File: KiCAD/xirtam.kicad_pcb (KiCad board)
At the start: 2 copper layers, 71.1 x 51.8 mm, 29 parts, among them J1 Exp Header, J2 Matrix, J3 Power, J4 JTAG, J5 Bootloader, P1 USB_A, SW1 Reset, U1 MT093APR1, U2 AT90USB1287, Y1 16 MHz Crystal

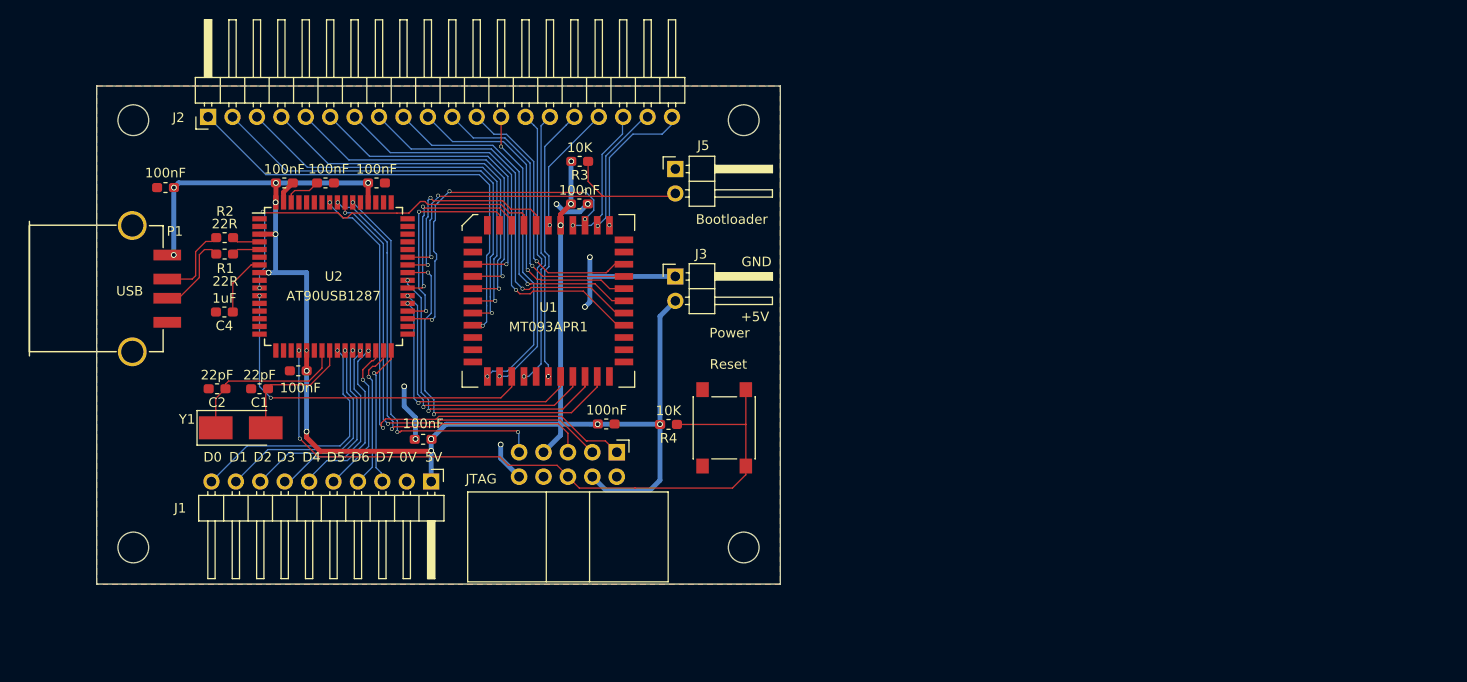
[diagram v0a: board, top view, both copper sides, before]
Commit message: Add in-line connector layout to PCB, no routing
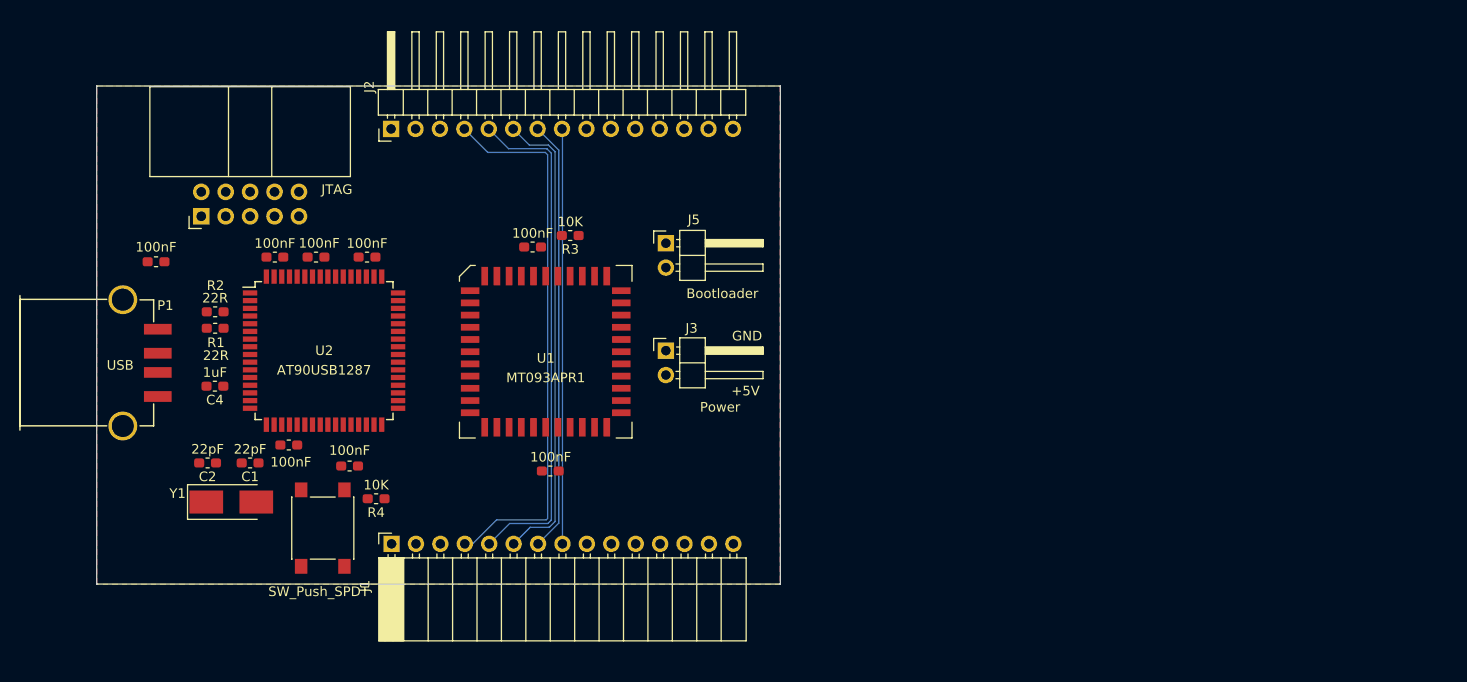
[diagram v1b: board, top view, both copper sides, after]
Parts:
- removed REF** (x4): MountingHole_3.2mm_M3, MountingHole:MountingHole_3.2mm_M3
- J1: value Exp Header -> Conn_01x15_Female; footprint Connector_PinHeader_2.54mm:PinHeader_1x10_P2.54mm_Horizontal -> Connector_PinSocket_2.54mm:PinSocket_1x15_P2.54mm_Horizontal
- J2: value Matrix -> Conn_01x15_Male; footprint Connector_PinHeader_2.54mm:PinHeader_1x20_P2.54mm_Horizontal -> Connector_PinHeader_2.54mm:PinHeader_1x15_P2.54mm_Horizontal
- SW1: value Reset -> SW_Push_SPDT
- moved J4 49.7 mm to (131.5, 93.8), turned to 90 degrees
- moved SW1 43.0 mm to (144.2, 126.3), turned to 90 degrees
- moved R4 31.4 mm to (149.7, 123.2)
- moved J2 19.1 mm to (151.3, 84.7)
- moved C8 8.14 mm to (147.0, 119.8)
- moved C6 7.78 mm to (140.6, 117.6)
- moved C9 7.78 mm to (126.8, 98.5)
- moved J3 7.78 mm to (179.9, 107.8)
- moved P1 7.78 mm to (125.5, 109.1)
- moved R1 7.78 mm to (133.0, 105.5)
- moved U2 7.78 mm to (144.3, 107.8)
- moved Y1 7.78 mm to (134.7, 123.5)
- moved R3 7.78 mm to (169.9, 95.8)
- moved C1 7.78 mm to (136.6, 119.5)
- moved C10 7.78 mm to (148.8, 98.1)
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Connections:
- J1 pad 1: +5V -> Net-(J1-Pad1)
- J1 pad 2: GND -> Net-(J1-Pad2)
- J2 pad 1: Net-(J2-Pad1) -> Net-(J1-Pad1)
- J2 pad 10: Net-(J2-Pad10) -> Net-(J1-Pad10)
- J2 pad 11: Net-(J2-Pad11) -> Net-(J1-Pad11)
- J2 pad 12: Net-(J2-Pad12) -> Net-(J1-Pad12)
- J2 pad 13: Net-(J2-Pad13) -> Net-(J1-Pad13)
- J2 pad 14: Net-(J2-Pad14) -> Net-(J1-Pad14)
- J2 pad 15: Net-(J2-Pad15) -> Net-(J1-Pad15)
- J2 pad 2: Net-(J2-Pad2) -> Net-(J1-Pad2)
- J2 pad 3: Net-(J2-Pad3) -> Net-(J1-Pad3)
- J2 pad 4: Net-(J2-Pad4) -> Net-(J1-Pad4)
- J2 pad 5: Net-(J2-Pad5) -> Net-(J1-Pad5)
- J2 pad 6: Net-(J2-Pad6) -> Net-(J1-Pad6)
- J2 pad 7: Net-(J2-Pad7) -> Net-(J1-Pad7)
- J2 pad 8: Net-(J2-Pad8) -> Net-(J1-Pad8)
- J2 pad 9: Net-(J2-Pad9) -> Net-(J1-Pad9)
- J4 pad 8: Net-(J4-Pad8) -> (no net)
- U1 pad 1: Net-(J2-Pad17) -> Net-(J1-Pad1)
- U1 pad 10: Net-(J2-Pad5) -> (no net)
- U1 pad 11: Net-(J2-Pad4) -> (no net)
- U1 pad 12: Net-(J2-Pad3) -> (no net)
- U1 pad 13: Net-(J2-Pad2) -> (no net)
- U1 pad 14: Net-(J2-Pad1) -> (no net)
- U1 pad 18: Net-(J2-Pad13) -> Net-(J1-Pad2)
- U1 pad 19: Net-(J2-Pad14) -> Net-(J1-Pad3)
- U1 pad 21: Net-(J2-Pad15) -> Net-(J1-Pad4)
- U1 pad 23: Net-(J2-Pad16) -> Net-(J1-Pad5)
- U1 pad 32: Net-(J2-Pad7) -> Net-(J1-Pad8)
- U1 pad 33: Net-(J2-Pad8) -> Net-(J1-Pad9)
- U1 pad 34: Net-(J2-Pad9) -> Net-(J1-Pad12)
- U1 pad 35: Net-(J2-Pad10) -> Net-(J1-Pad13)
- U1 pad 36: Net-(J2-Pad11) -> Net-(J1-Pad14)
- U1 pad 37: Net-(J2-Pad12) -> Net-(J1-Pad15)
- U1 pad 40: Net-(J2-Pad20) -> Net-(J1-Pad7)
- U1 pad 41: Net-(J2-Pad19) -> Net-(J1-Pad10)
- U1 pad 43: Net-(J2-Pad18) -> Net-(J1-Pad11)
- U1 pad 9: Net-(J2-Pad6) -> Net-(J1-Pad6)
- U2 pad 1: Net-(U2-Pad1) -> (no net)
- U2 pad 12: Net-(U2-Pad12) -> (no net)
- U2 pad 13: Net-(U2-Pad13) -> (no net)
- U2 pad 14: Net-(U2-Pad14) -> (no net)
- U2 pad 15: Net-(U2-Pad15) -> (no net)
- U2 pad 16: Net-(U2-Pad16) -> (no net)
- U2 pad 17: Net-(U2-Pad17) -> (no net)
- U2 pad 18: Net-(U2-Pad18) -> (no net)
- U2 pad 19: Net-(U2-Pad19) -> (no net)
- U2 pad 2: Net-(U2-Pad2) -> (no net)
- U2 pad 25: Net-(J1-Pad10) -> (no net)
- U2 pad 26: Net-(J1-Pad9) -> (no net)
- U2 pad 27: Net-(J1-Pad8) -> (no net)
- U2 pad 28: Net-(J1-Pad7) -> (no net)
- U2 pad 29: Net-(J1-Pad6) -> (no net)
- U2 pad 30: Net-(J1-Pad5) -> (no net)
- U2 pad 31: Net-(J1-Pad4) -> (no net)
- U2 pad 32: Net-(J1-Pad3) -> (no net)
- U2 pad 33: Net-(U2-Pad33) -> (no net)
- U2 pad 34: Net-(U2-Pad34) -> (no net)
- U2 pad 44: Net-(U2-Pad44) -> (no net)
- U2 pad 45: Net-(U2-Pad45) -> (no net)
- U2 pad 46: Net-(U2-Pad46) -> (no net)
- U2 pad 47: Net-(U2-Pad47) -> (no net)
- U2 pad 48: Net-(U2-Pad48) -> (no net)
- U2 pad 49: Net-(U2-Pad49) -> (no net)
- U2 pad 50: Net-(U2-Pad50) -> (no net)
- U2 pad 51: Net-(U2-Pad51) -> (no net)
- U2 pad 58: Net-(U2-Pad58) -> (no net)
- U2 pad 59: Net-(U2-Pad59) -> (no net)
- U2 pad 60: Net-(U2-Pad60) -> (no net)
- U2 pad 61: Net-(U2-Pad61) -> (no net)
- U2 pad 9: Net-(U2-Pad9) -> (no net)
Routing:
- net +5V: track 169.0 -> 0.00 mm, vias 18 -> 0
- net ~RESET: track 74.5 -> 0.00 mm, vias 2 -> 0
- net TCK: track 53.3 -> 0.00 mm, vias 2 -> 0
- net Net-(J2-Pad1): track 48.2 -> 0.00 mm, vias 1 -> 0
- net TDO: track 48.2 -> 0.00 mm, vias 2 -> 0
- net TMS: track 47.6 -> 0.00 mm, vias 2 -> 0
- net Net-(J2-Pad2): track 45.7 -> 0.00 mm, vias 1 -> 0
- net Net-(J2-Pad7): track 44.0 -> 0.00 mm, vias 1 -> 0
- net Net-(J2-Pad3): track 42.7 -> 0.00 mm, vias 1 -> 0
- net Net-(J1-Pad4): track 15.2 -> 57.3 mm, vias 1 -> 0
- net Net-(J2-Pad8): track 40.7 -> 0.00 mm, vias 1 -> 0
- net TDI: track 40.7 -> 0.00 mm, vias 3 -> 0
- net Net-(J2-Pad4): track 39.8 -> 0.00 mm, vias 1 -> 0
- net Net-(J5-Pad2): track 38.5 -> 0.00 mm, vias 2 -> 0
- net Net-(U1-Pad3): track 38.1 -> 0.00 mm, vias 2 -> 0
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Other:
- board text removed: "0V"
- board text removed: "5V"
- board text removed: "D0"
- board text removed: "D1"
- board text removed: "D2"
- board text removed: "D3"
- board text removed: "D4"
- board text removed: "D5"
- board text removed: "D6"
- board text removed: "D7"

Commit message: New PCB layout
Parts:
- removed the C7 at (167.8, 120.3)
- removed the C8 at (147.0, 119.8)
- removed C9: 100nF, Capacitor_SMD:C_0603_1608Metric_Pad1.05x0.95mm_HandSolder
- added J6: Debug, Connector_PinHeader_2.54mm:PinHeader_1x04_P2.54mm_Horizontal, F.Cu at (170.7, 121.1)
- added M1: MatrixInterconnectMatrix, Jumper:matrixinterconnectmatrix, F.Cu at (182.0, 88.6)
- added REF**: MountingHole_2.2mm_M2, MountingHole:MountingHole_2.2mm_M2, F.Cu at (123.4, 82.8)
- added REF**: MountingHole_2.2mm_M2, MountingHole:MountingHole_2.2mm_M2, F.Cu at (123.4, 129.5)
- added REF**: MountingHole_2.2mm_M2, MountingHole:MountingHole_2.2mm_M2, F.Cu at (258.6, 129.6)
- added REF**: MountingHole_2.2mm_M2, MountingHole:MountingHole_2.2mm_M2, F.Cu at (258.5, 82.9)
- J1: value Conn_01x15_Female -> Conn_01x28_Male; footprint Connector_PinSocket_2.54mm:PinSocket_1x15_P2.54mm_Horizontal -> Connector_PinHeader_2.54mm:PinHeader_1x28_P2.54mm_Horizontal
- J2: value Conn_01x15_Male -> Conn_01x28_Female; footprint Connector_PinHeader_2.54mm:PinHeader_1x15_P2.54mm_Horizontal -> Connector_PinSocket_2.54mm:PinSocket_1x28_P2.54mm_Horizontal
- SW1: value SW_Push_SPDT -> Reset; footprint Button_Switch_SMD:SW_Push_1P1T_NO_6x6mm_H9.5mm -> Button_Switch_SMD:SW_SPST_FSMSM
- Y1: value 16 MHz Crystal -> 16 MHz
- moved J2 56.7 mm to (185.3, 130.1)
- moved J1 54.9 mm to (185.3, 84.9)
- moved J5 27.7 mm to (152.7, 91.2), turned to 90 degrees
- moved J3 21.7 mm to (165.9, 91.2), turned to 90 degrees
- moved R3 15.5 mm to (154.4, 95.5)
- moved SW1 6.26 mm to (150.2, 127.9), turned to 0 degrees
- moved R4 2.44 mm to (150.0, 120.8)
- moved C8 1.87 mm to (167.8, 97.6), turned to 0 degrees
- moved C3 0.49 mm to (143.0, 98.0)
- renumbered C10 to C7, C11 to C8
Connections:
- J2 pad 1: Net-(J1-Pad1) -> Net-(J2-Pad1)
- J2 pad 10: Net-(J1-Pad10) -> Net-(J2-Pad10)
- J2 pad 11: Net-(J1-Pad11) -> Net-(J2-Pad11)
- J2 pad 12: Net-(J1-Pad12) -> Net-(J2-Pad12)
- J2 pad 13: Net-(J1-Pad13) -> Net-(J2-Pad13)
- J2 pad 14: Net-(J1-Pad14) -> Net-(J2-Pad14)
- J2 pad 15: Net-(J1-Pad15) -> Net-(J2-Pad15)
- J2 pad 2: Net-(J1-Pad2) -> Net-(J2-Pad2)
- J2 pad 3: Net-(J1-Pad3) -> Net-(J2-Pad3)
- J2 pad 4: Net-(J1-Pad4) -> Net-(J2-Pad4)
- J2 pad 5: Net-(J1-Pad5) -> Net-(J2-Pad5)
- J2 pad 6: Net-(J1-Pad6) -> Net-(J2-Pad6)
- J2 pad 7: Net-(J1-Pad7) -> Net-(J2-Pad7)
- J2 pad 8: Net-(J1-Pad8) -> Net-(J2-Pad8)
- J2 pad 9: Net-(J1-Pad9) -> Net-(J2-Pad9)
- SW1 pad 1: ~RESET -> GND
- SW1 pad 2: GND -> ~RESET
- U1 pad 1: Net-(J1-Pad1) -> Net-(M1-Pad4)
- U1 pad 10: (no net) -> Net-(M1-Pad16)
- U1 pad 11: (no net) -> Net-(M1-Pad17)
- U1 pad 12: (no net) -> Net-(M1-Pad18)
- U1 pad 13: (no net) -> Net-(M1-Pad19)
- U1 pad 14: (no net) -> Net-(M1-Pad20)
- U1 pad 18: Net-(J1-Pad2) -> Net-(M1-Pad8)
- U1 pad 19: Net-(J1-Pad3) -> Net-(M1-Pad7)
- U1 pad 21: Net-(J1-Pad4) -> Net-(M1-Pad6)
- U1 pad 23: Net-(J1-Pad5) -> Net-(M1-Pad5)
- U1 pad 32: Net-(J1-Pad8) -> Net-(M1-Pad14)
- U1 pad 33: Net-(J1-Pad9) -> Net-(M1-Pad13)
- U1 pad 34: Net-(J1-Pad12) -> Net-(M1-Pad12)
- U1 pad 35: Net-(J1-Pad13) -> Net-(M1-Pad11)
- U1 pad 36: Net-(J1-Pad14) -> Net-(M1-Pad10)
- U1 pad 37: Net-(J1-Pad15) -> Net-(M1-Pad9)
- U1 pad 40: Net-(J1-Pad7) -> Net-(M1-Pad1)
- U1 pad 41: Net-(J1-Pad10) -> Net-(M1-Pad2)
- U1 pad 43: Net-(J1-Pad11) -> Net-(M1-Pad3)
- U1 pad 9: Net-(J1-Pad6) -> Net-(M1-Pad15)
- U2 pad 10: Net-(U1-Pad3) -> (no net)
- U2 pad 11: Net-(U1-Pad20) -> (no net)
- U2 pad 25: (no net) -> Net-(U1-Pad20)
- U2 pad 26: (no net) -> Net-(U1-Pad42)
- U2 pad 27: (no net) -> /RxD
- U2 pad 28: (no net) -> /TxD
- U2 pad 29: (no net) -> Net-(U1-Pad3)
- U2 pad 35: Net-(U1-Pad42) -> Net-(U1-Pad5)
- U2 pad 36: Net-(U1-Pad5) -> Net-(U1-Pad24)
- U2 pad 37: Net-(U1-Pad24) -> Net-(U1-Pad25)
- U2 pad 38: Net-(U1-Pad25) -> Net-(U1-Pad4)
- U2 pad 39: Net-(U1-Pad4) -> Net-(U1-Pad26)
- U2 pad 40: Net-(U1-Pad26) -> Net-(U1-Pad27)
- U2 pad 41: Net-(U1-Pad27) -> Net-(U1-Pad2)
- U2 pad 42: Net-(U1-Pad2) -> (no net)
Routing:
- net +5V: track 0.00 -> 152.4 mm, vias 0 -> 2
- net GND: track 0.00 -> 99.3 mm, vias 0 -> 37
- net Net-(J1-Pad4): track 57.3 -> 3.02 mm
- net ~RESET: track 0.00 -> 51.1 mm, vias 0 -> 1
- net Net-(J1-Pad5): track 53.2 -> 3.02 mm
- net Net-(J1-Pad6): track 49.1 -> 3.02 mm
- net Net-(J1-Pad7): track 45.0 -> 3.02 mm
- net Net-(J1-Pad8): track 43.2 -> 3.02 mm
- net Net-(U1-Pad42): track 0.00 -> 38.2 mm, vias 0 -> 2
- net Net-(M1-Pad8): track 0.00 -> 30.9 mm, vias 0 -> 1
- net Net-(U1-Pad3): track 0.00 -> 30.1 mm, vias 0 -> 2
- net Net-(M1-Pad7): track 0.00 -> 29.9 mm, vias 0 -> 1
- net Net-(M1-Pad6): track 0.00 -> 28.6 mm, vias 0 -> 1
- net Net-(M1-Pad5): track 0.00 -> 27.8 mm, vias 0 -> 1
- net Net-(M1-Pad20): track 0.00 -> 25.6 mm, vias 0 -> 1
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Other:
- board size 71.1 x 51.8 mm -> 140.3 x 51.9 mm
- board text added: "10"
- board text added: "15"
- board text added: "20"
- board text added: "25"
- board text added: "5"
- board text added: "5V"
- board text added: "RxD"
- board text added: "TxD"

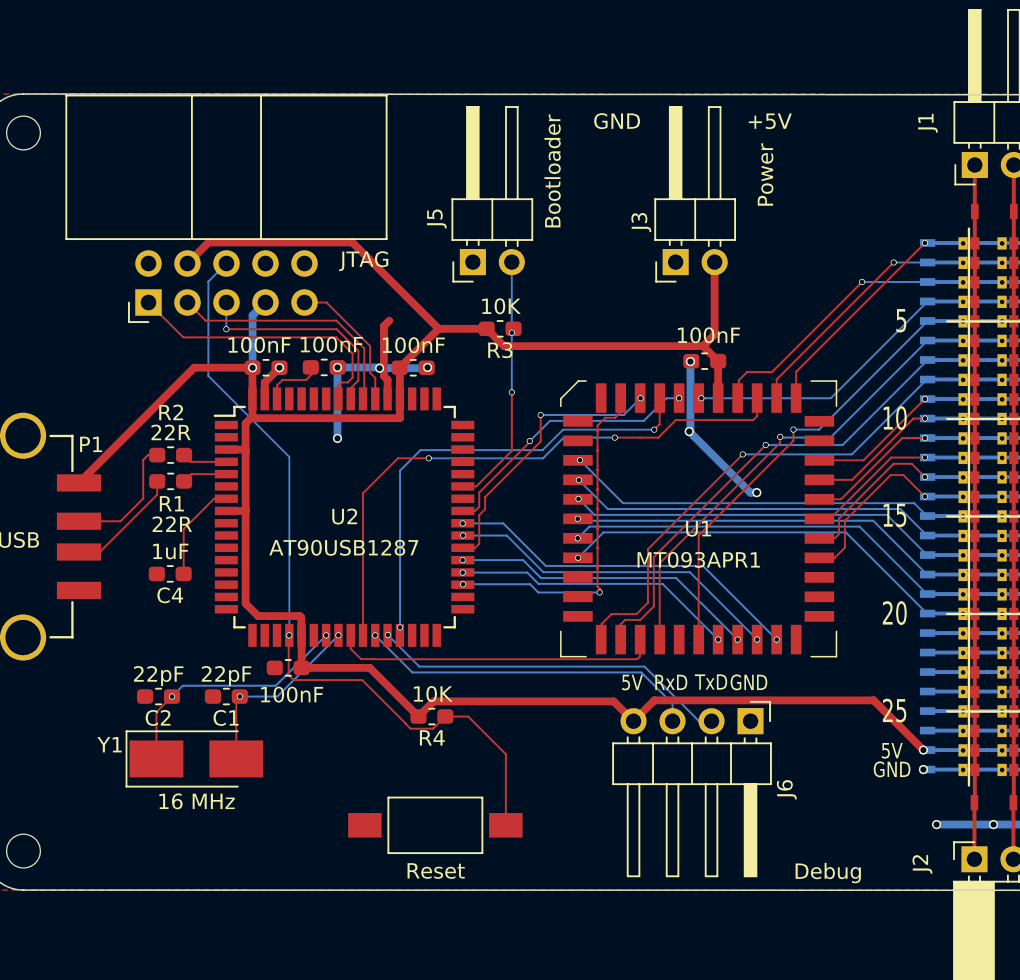
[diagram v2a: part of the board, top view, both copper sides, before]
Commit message: New layout, updated schematic
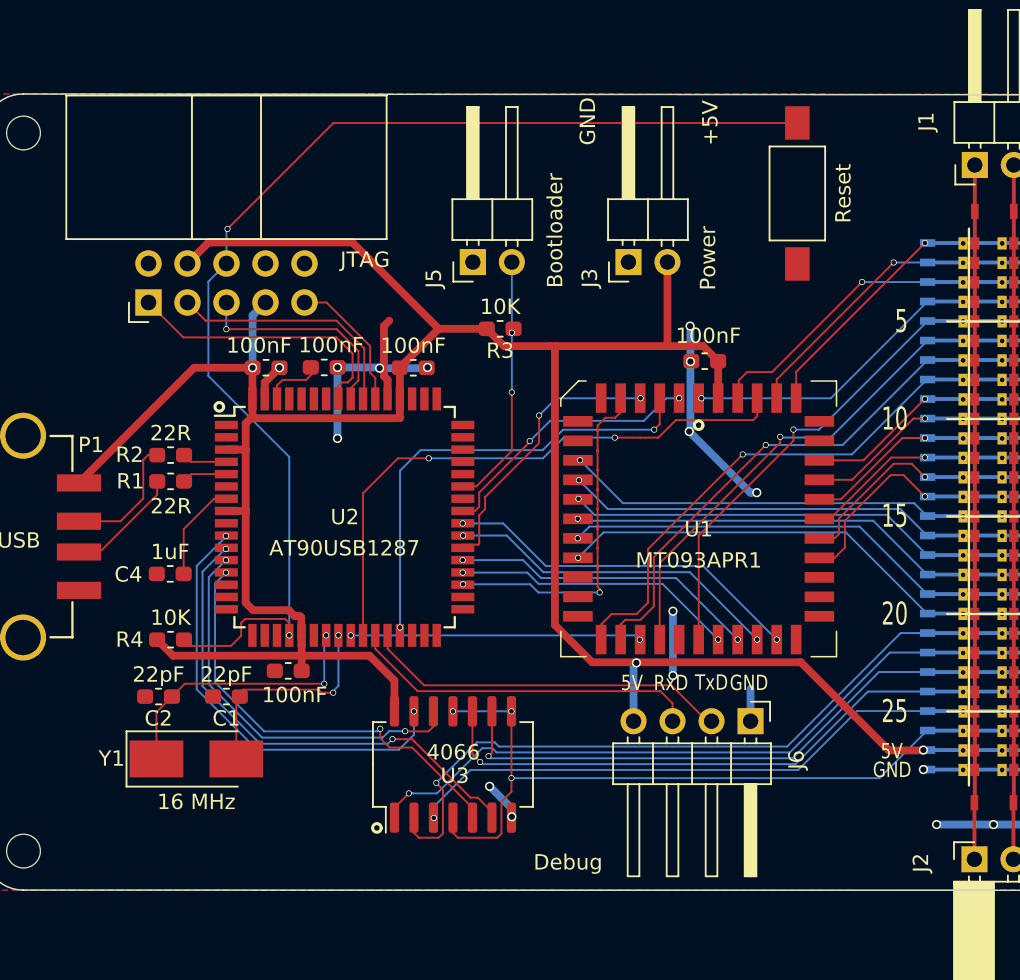
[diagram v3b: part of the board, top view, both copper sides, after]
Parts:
- added U3: 4066, Package_SO:SO-14_5.3x10.2mm_P1.27mm, F.Cu at (151.4, 123.9)
- moved SW1 47.4 mm to (173.8, 86.7), turned to 90 degrees
- moved R4 17.7 mm to (133.0, 115.8)
- moved J3 3.07 mm to (162.8, 91.2)
- moved C6 0.20 mm to (140.6, 117.8)
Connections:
- net /RxD renamed RxD
- net /TxD renamed TxD
- M1 pad 21: (no net) -> Net-(M1-Pad21)
- M1 pad 22: (no net) -> Net-(M1-Pad22)
- M1 pad 23: (no net) -> Net-(M1-Pad23)
- M1 pad 24: (no net) -> Net-(M1-Pad24)
- M1 pad 25: (no net) -> Net-(M1-Pad25)
- M1 pad 26: (no net) -> Net-(M1-Pad26)
- U2 pad 10: (no net) -> AUX1
- U2 pad 11: (no net) -> AUX2
- U2 pad 12: (no net) -> AUX3
- U2 pad 13: (no net) -> AUX4
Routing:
- net Net-(M1-Pad26): track 0.00 -> 44.8 mm, vias 0 -> 3
- net Net-(M1-Pad21): track 0.00 -> 42.8 mm, vias 0 -> 1
- net Net-(M1-Pad22): track 0.00 -> 39.7 mm, vias 0 -> 1
- net Net-(M1-Pad25): track 0.00 -> 35.5 mm, vias 0 -> 1
- net Net-(M1-Pad24): track 0.00 -> 34.6 mm, vias 0 -> 1
- net Net-(M1-Pad23): track 0.00 -> 34.0 mm, vias 0 -> 1
- net AUX2: track 0.00 -> 32.7 mm, vias 0 -> 2
- net AUX4: track 0.00 -> 28.8 mm, vias 0 -> 2
- net AUX1: track 0.00 -> 28.5 mm, vias 0 -> 2
- net ~RESET: track 51.1 -> 78.5 mm, vias 1 -> 2
- net AUX3: track 0.00 -> 25.9 mm, vias 0 -> 2
- net +5V: track 152.4 -> 175.5 mm, vias 2 -> 3
- net GND: track 99.3 -> 110.5 mm, vias 37 -> 42
- net Net-(C1-Pad1): track 12.2 -> 14.5 mm
- net Net-(U1-Pad20): track 21.2 -> 19.0 mm, vias 0 -> 2
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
